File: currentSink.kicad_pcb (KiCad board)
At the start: 2 copper layers, 0 parts

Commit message: removed duplicates and bad wire connections to enable the generation of a PCB
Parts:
- added C201: C, Capacitors_SMD:C_0805_HandSoldering, F.Cu at (144.3, 114.5)
- added C301: C, Capacitors_SMD:C_0805_HandSoldering, F.Cu at (202.1, 126.2)
- added C302: 100nF, Capacitors_SMD:C_0805_HandSoldering, F.Cu at (202.2, 132.5)
- added C401: 0.1uF, Capacitors_SMD:C_0805_HandSoldering, F.Cu at (184.5, 103.6)
- added C402: 4.7uF, Capacitors_SMD:C_0805_HandSoldering, F.Cu at (179.2, 109.9)
- added C403: 100uF, Capacitors_SMD:C_0805_HandSoldering, F.Cu at (184.4, 109.9)
- added C404: 10uF, Capacitors_SMD:C_0805_HandSoldering, F.Cu at (189.5, 103.6)
- added C501: 0.1uF, Capacitors_SMD:C_0805_HandSoldering, F.Cu at (173.7, 126.3)
- added C502: 10uF, Capacitors_SMD:C_0805_HandSoldering, F.Cu at (173.7, 132.6)
- added C601: 100nf, Capacitors_SMD:C_0805_HandSoldering, F.Cu at (167.2, 149.2)
- added C602: 100nf, Capacitors_SMD:C_0805_HandSoldering, F.Cu at (172.5, 142.9)
- added D301: IN4148, SMD_Packages:SOD-523, F.Cu at (188.5, 132.8)
- added L401: 4.7uH, Resistors_SMD:R_0805_HandSoldering, F.Cu at (178.2, 116.2)
- added P101: ExtBatt_Power, Pin_Headers:Pin_Header_Straight_1x02, F.Cu at (142.9, 129.3)
- added P102: uPower, Pin_Headers:Pin_Header_Straight_1x02, F.Cu at (151.4, 129.3)
- added P103: uSignals, Pin_Headers:Pin_Header_Straight_1x05, F.Cu at (124.1, 129.3)
- added P104: Load+ve, Pin_Headers:Pin_Header_Straight_1x01, F.Cu at (147.8, 140.1)
- added P105: Load-ve, Pin_Headers:Pin_Header_Straight_1x01, F.Cu at (140.8, 140.1)
- added P106: PowerSwitch, Pin_Headers:Pin_Header_Straight_1x03, F.Cu at (132.5, 129.3)
- added P201: TST, Measurement_Points:Measurement_Point_Round-TH_Small, F.Cu at (129.1, 115.0)
- added P202: TST, Measurement_Points:Measurement_Point_Round-TH_Small, F.Cu at (151.5, 104.0)
- added P301: TST, Measurement_Points:Measurement_Point_Round-TH_Small, F.Cu at (192.1, 126.6)
- added P302: TST, Measurement_Points:Measurement_Point_Round-TH_Small, F.Cu at (187.7, 126.6)
- added P401: TST, Measurement_Points:Measurement_Point_Round-TH_Small, F.Cu at (169.3, 104.0)
- added Q201: BUK9575, Transistors_TO-220:TO-220_FET-GDS_Vertical, F.Cu at (143.6, 106.5)
- added R201: R, Resistors_SMD:R_0805_HandSoldering, F.Cu at (133.9, 113.4)
- added R202: .1, Resistors_ThroughHole:Resistor_Horizontal_RM15mm, F.Cu at (129.3, 105.2)
- added R203: 5.6k, Resistors_SMD:R_0805_HandSoldering, F.Cu at (151.9, 110.7)
- added R204: 1k, Resistors_SMD:R_0805_HandSoldering, F.Cu at (139.1, 117.0)
- added R301: 19.1K, Resistors_SMD:R_0805_HandSoldering, F.Cu at (197.0, 126.2)
- added R302: 2.2k, Resistors_SMD:R_0805_HandSoldering, F.Cu at (197.0, 132.5)
- added R401: 0, Resistors_SMD:R_0805_HandSoldering, F.Cu at (173.0, 116.2)
- added R402: 27K, Resistors_SMD:R_0805_HandSoldering, F.Cu at (179.3, 103.6)
- added R403: 21.6K, Resistors_SMD:R_0805_HandSoldering, F.Cu at (174.1, 109.9)
- added R404: 976K, Resistors_SMD:R_0805_HandSoldering, F.Cu at (167.7, 111.5)
- added R405: 562K, Resistors_SMD:R_0805_HandSoldering, F.Cu at (174.1, 103.6)
- added R601: 10K, Resistors_SMD:R_0805_HandSoldering, F.Cu at (167.3, 142.9)
- added U201: LMV358, SMD_Packages:SOIC-8-N, F.Cu at (123.8, 114.1)
- added U401: LM2931, Power_Integrations:SO-8, F.Cu at (162.0, 112.0)
- added U402: MCP1640T, Housings_SOT-23_SOT-143_TSOT-6:SOT-23-6, F.Cu at (162.9, 104.4)
- added U501: MCP4802-E/SN, SMD_Packages:SOIC-8-N, F.Cu at (164.8, 127.1)
- added U601: ACS711, SMD_Packages:SOIC-8-N, F.Cu at (161.6, 143.6)

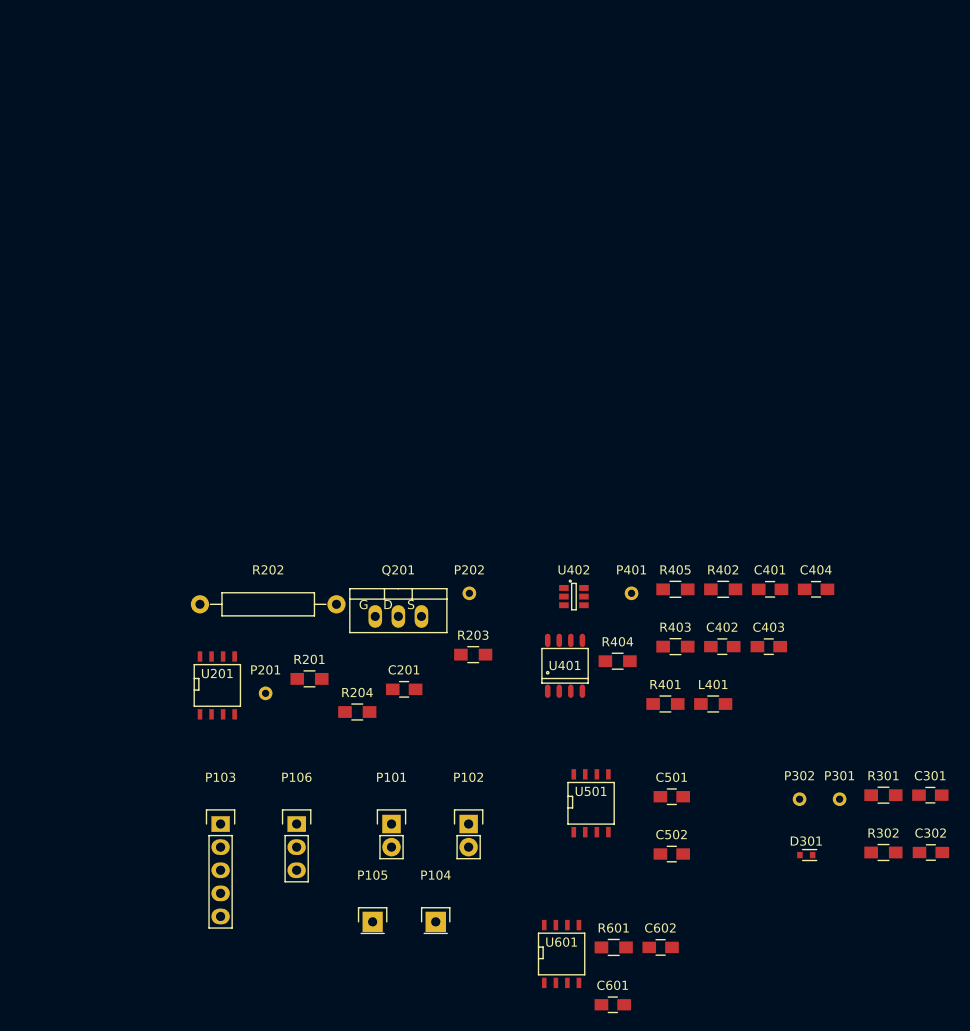
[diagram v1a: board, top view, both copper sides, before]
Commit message: initial layout complete with gnd plane
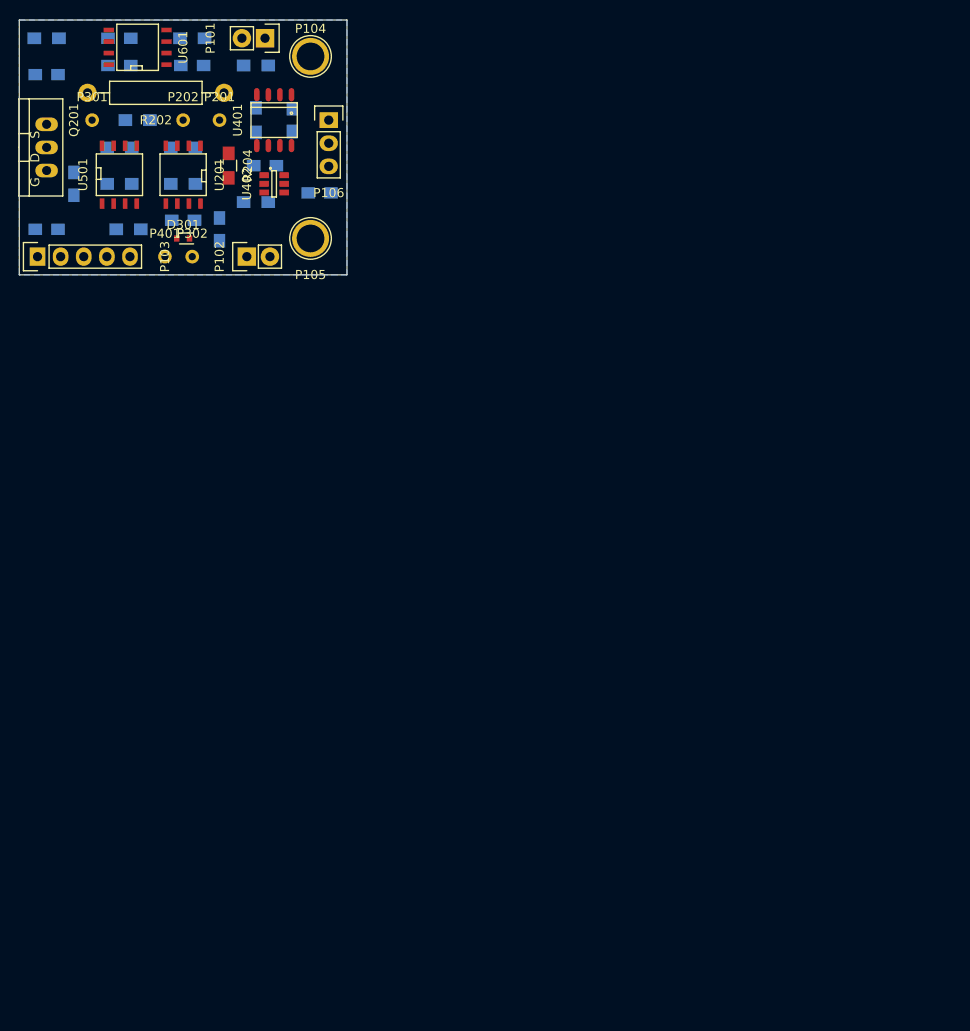
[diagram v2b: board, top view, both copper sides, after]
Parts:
- C201, C301, C302, C401, C402, C403, C404, C501, C502, C601, C602, L401, R201, R203, R301, R302, R401, R402, R403, R404, R405, R601: moved to B.Cu
- P104, P105: footprint Pin_Headers:Pin_Header_Straight_1x01 -> Connect:1pin
- moved C301 121.9 mm to (113.0, 43.0)
- moved R601 117.7 mm to (105.0, 43.0), turned to 180 degrees
- moved R302 111.6 mm to (113.0, 59.0)
- moved P301 111.0 mm to (110.0, 52.0)
- moved R301 110.1 mm to (113.0, 55.0)
- moved U601 110.0 mm to (115.0, 44.0), turned to 90 degrees
- moved C302 107.6 mm to (120.0, 63.0)
- moved C601 105.5 mm to (105.0, 64.0)
- moved C404 101.7 mm to (105.0, 47.0), turned to 180 degrees
- moved D301 96.3 mm to (120.0, 65.0)
- moved C602 96.3 mm to (129.0, 57.0)
- moved P104 96.1 mm to (134.0, 45.0)
- moved C501 94.1 mm to (108.0, 59.0), turned to 90 degrees
- moved C402 92.0 mm to (113.0, 46.0)
- moved C403 90.0 mm to (121.0, 46.0)
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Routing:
- added copper zone on B.Cu, net GND
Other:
- board outline added: 36 x 28 mm

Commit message: updated with some of the frontside tracks
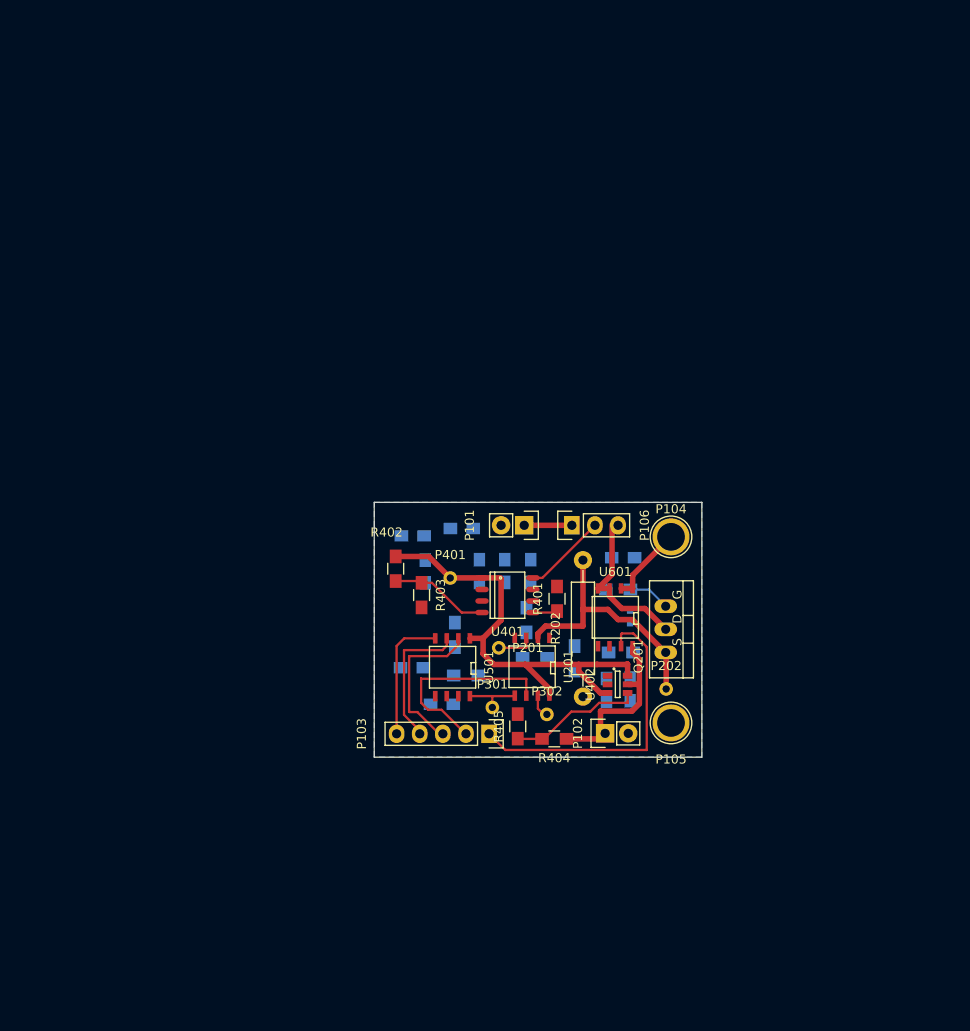
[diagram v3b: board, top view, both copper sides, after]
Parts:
- D301, R204: moved to B.Cu
- R401, R402, R403, R404, R405: moved to F.Cu
- moved C404 93.1 mm to (169.1, 114.6), turned to 90 degrees
- moved R601 92.4 mm to (168.1, 110.5)
- moved Q201 86.2 mm to (173.0, 108.0), turned to 270 degrees
- moved P202 82.0 mm to (173.1, 114.5)
- moved U601 81.7 mm to (167.5, 106.6), turned to 180 degrees
- moved P301 78.1 mm to (154.0, 116.5)
- moved R202 75.3 mm to (163.9, 107.8), turned to 270 degrees
- moved R203 73.5 mm to (158.6, 111.1)
- moved P103 72.2 mm to (153.6, 119.4), turned to 270 degrees
- moved C402 71.6 mm to (158.2, 101.5), turned to 270 degrees
- moved R405 70.0 mm to (156.8, 118.6), turned to 90 degrees
- moved C602 68.7 mm to (166.5, 114.6), turned to 90 degrees
- moved L401 68.7 mm to (163.0, 111.2), turned to 90 degrees
- moved R201 68.1 mm to (167.8, 103.6), turned to 180 degrees
- moved C601 67.9 mm to (148.4, 116.2), turned to 180 degrees
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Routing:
- net 2.7V: track 0.00 -> 50.3 mm
- net /Current Read/Current_Read: track 0.00 -> 34.2 mm
- net Net-(P202-Pad1): track 0.00 -> 28.4 mm
- net /Voltage Control/VoltageRead: track 0.00 -> 22.4 mm
- net 3.3V: track 0.00 -> 19.3 mm
- net /Current Read/CurrentSink_Out: track 0.00 -> 17.5 mm
- net /Micro Control/~CS: track 0.00 -> 17.5 mm
- net /Micro Control/SCK: track 0.00 -> 15.6 mm
- net Net-(R404-Pad2): track 0.00 -> 14.8 mm
- net /Micro Control/SDI: track 0.00 -> 14.2 mm
- net Net-(R402-Pad2): track 0.00 -> 10.9 mm
- net /Power Regulation/Vin: track 0.00 -> 9.21 mm
- net /Current Read/CurrentSink_In: track 0.00 -> 8.68 mm
- net /Voltage Control/DAC_Va: track 0.00 -> 6.24 mm
- net Net-(P101-Pad1): track 0.00 -> 5.23 mm
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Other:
- net class Default: clearance 0.2 -> 0.254; trace_width 0.25 -> 0.254; via_dia 0.6 -> 0.889; via_drill 0.4 -> 0.635
- net class Power added: clearance 0.3048, trace_width 0.6096, via_dia 1.143, via_drill 0.762
- rule trace_clearance: 0.2 -> 0.254

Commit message: updated layout - note not optimised
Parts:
- moved R301 14.4 mm to (158.2, 120.2), turned to 180 degrees
- moved R204 9.01 mm to (149.1, 109.7), turned to 180 degrees
- moved R203 8.48 mm to (150.6, 113.7), turned to 270 degrees
- moved R302 7.46 mm to (158.2, 115.1)
- moved D301 6.62 mm to (163.6, 110.3)
- moved C601 5.72 mm to (142.8, 115.0), turned to 90 degrees
- moved L401 3.61 mm to (159.8, 109.5)
- moved R601 3.10 mm to (168.2, 107.4)
- moved C302 3.09 mm to (146.6, 114.9), turned to 90 degrees
- moved C404 2.44 mm to (168.2, 112.3), turned to 180 degrees
- moved U601 1.76 mm to (167.1, 104.9)
- moved C602 1.66 mm to (168.0, 115.4), turned to 180 degrees
- moved R202 1.65 mm to (162.3, 108.2)
- moved C401 1.50 mm to (166.9, 100.4), turned to 180 degrees
- moved P301 1.02 mm to (153.0, 116.6)
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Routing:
- net GND: track 0.00 -> 106.1 mm, vias 0 -> 8
- net /Current Read/CurrentSink_Out: track 17.5 -> 49.2 mm
- net 2.7V: track 50.3 -> 75.5 mm, vias 0 -> 1
- net /Current Read/Current_Read: track 34.2 -> 55.3 mm
- net /Voltage Control/VoltageRead: track 22.4 -> 40.9 mm, vias 0 -> 1
- net /Current Control/FET_Gate: track 4.64 -> 18.8 mm
- net Net-(D301-Pad2): track 2.68 -> 14.7 mm
- net 3.3V: track 19.3 -> 29.8 mm, vias 0 -> 1
- net Net-(R201-Pad2): track 0.00 -> 10.5 mm, vias 0 -> 1
- net Net-(L401-Pad2): track 0.00 -> 9.73 mm, vias 0 -> 1
- net Net-(P201-Pad1): track 4.10 -> 13.5 mm
- net /Power Regulation/Vin: track 9.21 -> 16.3 mm
- net /Current Control/DAC_Vb: track 0.00 -> 4.57 mm, vias 0 -> 1
- net Net-(R601-Pad2): track 0.00 -> 4.42 mm, vias 0 -> 1
- net Net-(P202-Pad1): track 28.4 -> 31.4 mm
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
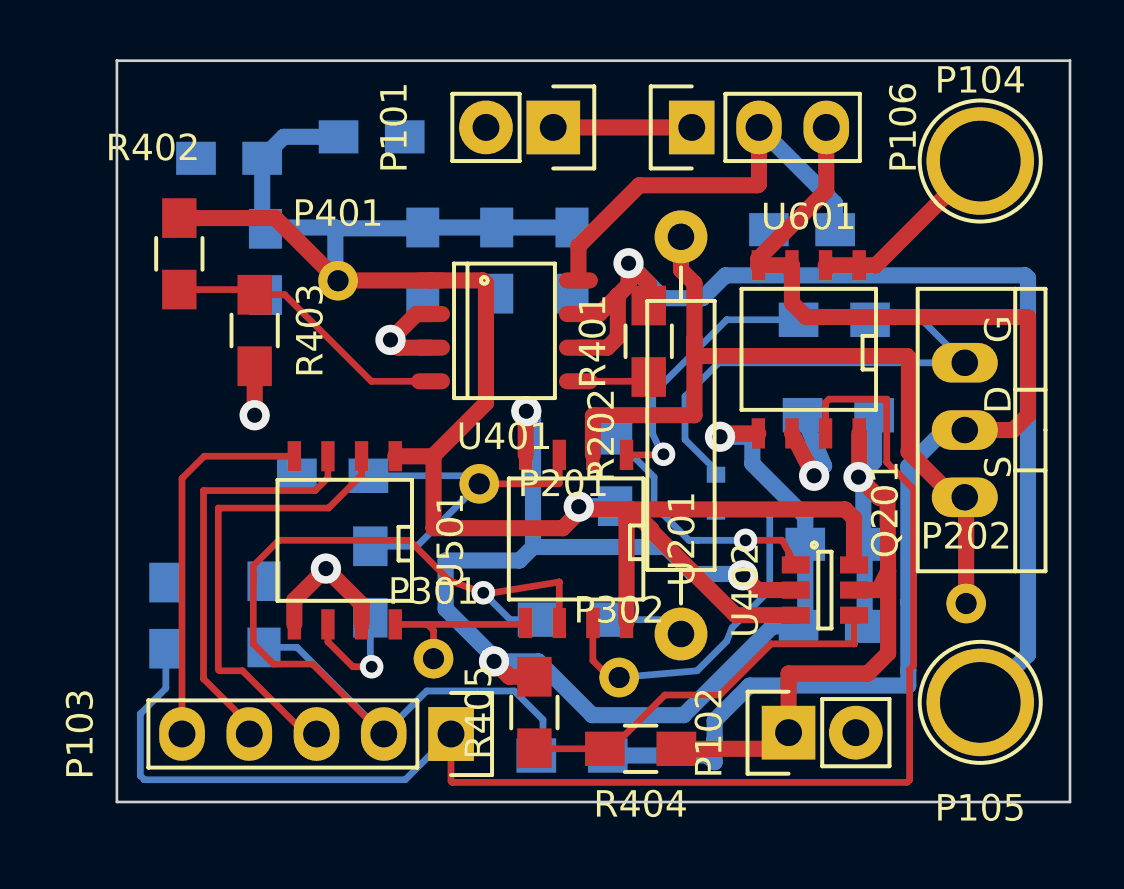
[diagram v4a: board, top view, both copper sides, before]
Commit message: updated layout. DRC has 4 footprint errors for U402 however measurements appear OK to datasheet
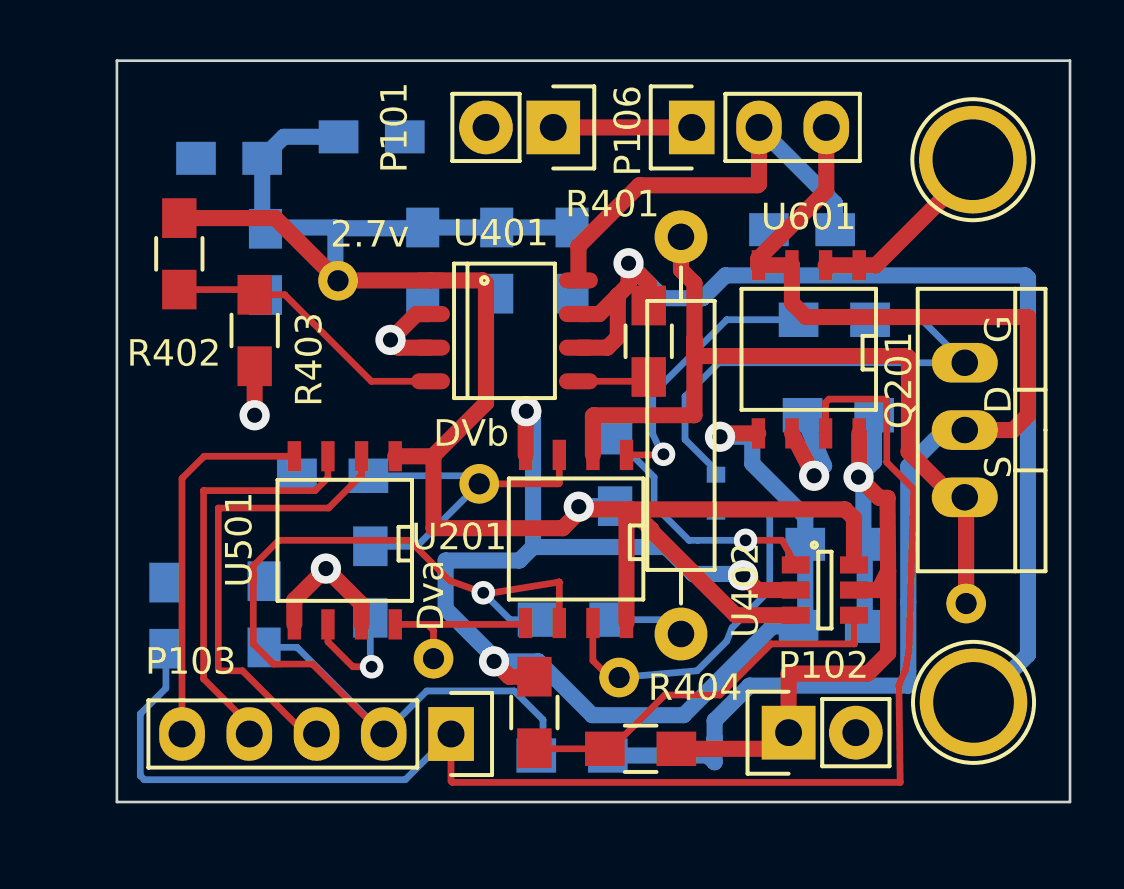
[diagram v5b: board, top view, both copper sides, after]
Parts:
- moved P104 0.28 mm to (173.3, 97.7)
- moved P105 0.25 mm to (173.4, 118.2)
- renumbered P401 to 2.7v, P201 to DVb, P301 to Dva
